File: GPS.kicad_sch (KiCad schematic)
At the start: 14 parts, among them Q5 Q_NMOS_DGS, Q6 Q_PMOS_DGS, U10 L96-M33

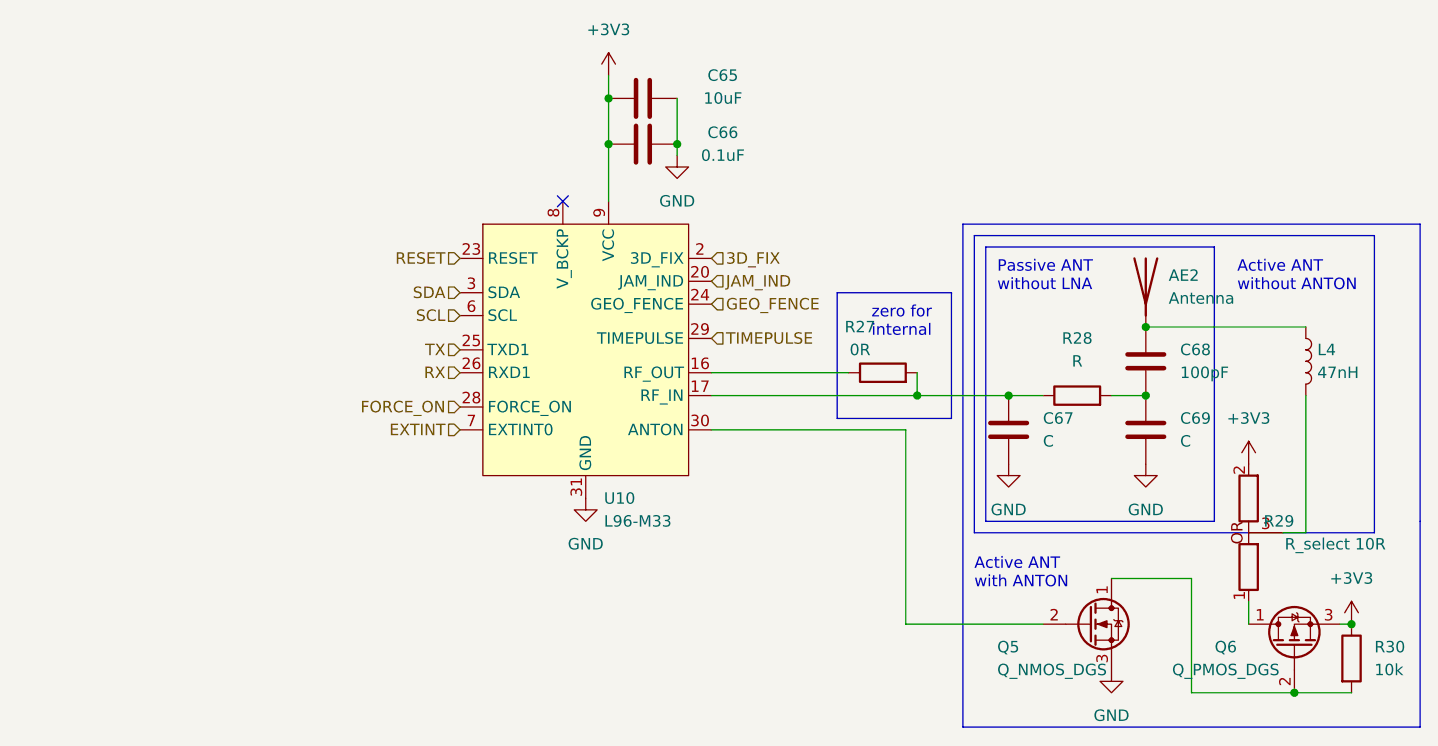
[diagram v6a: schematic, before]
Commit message: added nfc antenna components, added most of footprints
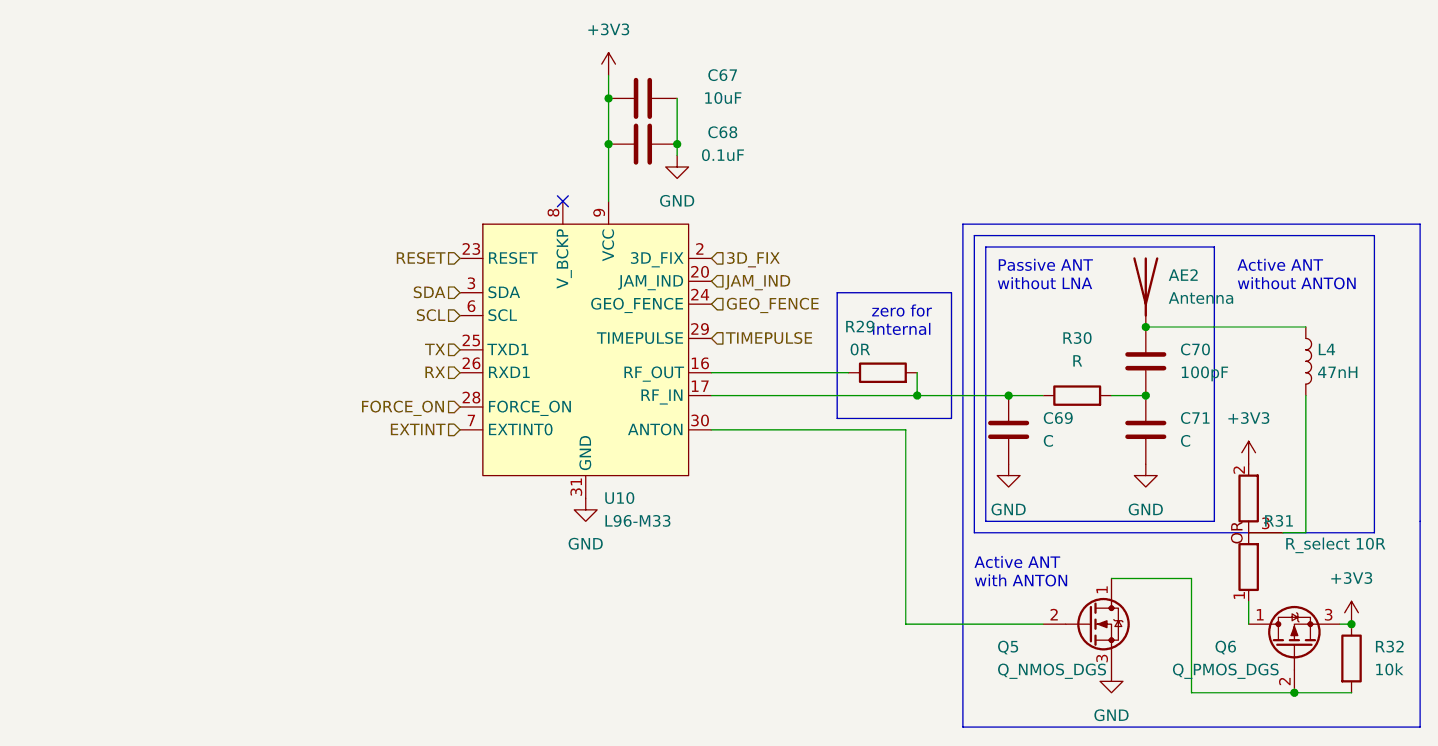
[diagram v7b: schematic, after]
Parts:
- AE2: footprint (none) -> Connector_Coaxial:U.FL_Molex_MCRF_73412-0110_Vertical
- C68: renamed from C66; footprint (none) -> Capacitor_SMD:C_0603_1608Metric_Pad1.08x0.95mm_HandSolder
- C69: renamed from C67; footprint (none) -> Capacitor_SMD:C_0603_1608Metric_Pad1.08x0.95mm_HandSolder
- C70: renamed from C68; footprint (none) -> Capacitor_SMD:C_0603_1608Metric_Pad1.08x0.95mm_HandSolder
- C71: renamed from C69; footprint (none) -> Capacitor_SMD:C_0603_1608Metric_Pad1.08x0.95mm_HandSolder
- R30: renamed from R28; footprint (none) -> Resistor_SMD:R_0603_1608Metric
- R31: renamed from R29; footprint (none) -> airsoft_controller:0603-R-select
- R32: renamed from R30; footprint (none) -> Resistor_SMD:R_0603_1608Metric
- U10: footprint airsoft_controller:L29 -> airsoft_controller:L96
- renumbered C65 to C67, R27 to R29
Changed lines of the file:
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@@
   (symbol (lib_id "Device:R") (at 172.72 90.17 90) (unit 1)
     (in_bom yes) (on_board yes)
-    (property "Reference" "R27" (id 0) (at 170.18 85.09 90))
+    (property "Reference" "R29" (id 0) (at 170.18 85.09 90))
     (property "Value" "0R" (id 1) (at 170.18 87.63 90))
     (property "Footprint" "" (id 2) (at 172.72 91.948 90)
@@
   (symbol (lib_id "Device:C") (at 201.93 88.9 180) (unit 1)
     (in_bom yes) (on_board yes)
-    (property "Reference" "C68" (id 0) (at 205.74 87.6299 0)
+    (property "Reference" "C70" (id 0) (at 205.74 87.6299 0)
       (effects (font (size 1.27 1.27)) (justify right))
     )
@@
       (effects (font (size 1.27 1.27)) (justify right))
     )
-    (property "Footprint" "" (id 2) (at 200.9648 85.09 0)
+    (property "Footprint" "Capacitor_SMD:C_0603_1608Metric_Pad1.08x0.95mm_HandSolder" (id 2) (at 200.9648 85.09 0)
       (effects (font (size 1.27 1.27)) hide)
     )
@@
   (symbol (lib_id "Device:C") (at 146.05 64.77 270) (mirror x) (unit 1)
     (in_bom yes) (on_board yes)
-    (property "Reference" "C66" (id 0) (at 154.94 63.5 90))
+    (property "Reference" "C68" (id 0) (at 154.94 63.5 90))
     (property "Value" "0.1uF" (id 1) (at 154.94 66.04 90))
-    (property "Footprint" "" (id 2) (at 142.24 63.8048 0)
+    (property "Footprint" "Capacitor_SMD:C_0603_1608Metric_Pad1.08x0.95mm_HandSolder" (id 2) (at 142.24 63.8048 0)
       (effects (font (size 1.27 1.27)) hide)
     )
@@
       (effects (font (size 1.27 1.27)) (justify left))
     )
-    (property "Footprint" "" (id 2) (at 201.93 80.01 0)
+    (property "Footprint" "Connector_Coaxial:U.FL_Molex_MCRF_73412-0110_Vertical" (id 2) (at 201.93 80.01 0)
       (effects (font (size 1.27 1.27)) hide)
     )
@@
   (symbol (lib_id "Device:C") (at 201.93 96.52 0) (unit 1)
     (in_bom yes) (on_board yes) (fields_autoplaced)
-    (property "Reference" "C69" (id 0) (at 205.74 95.2499 0)
+    (property "Reference" "C71" (id 0) (at 205.74 95.2499 0)
       (effects (font (size 1.27 1.27)) (justify left))
     )
@@
       (effects (font (size 1.27 1.27)) (justify left))
     )
-    (property "Footprint" "" (id 2) (at 202.8952 100.33 0)
+    (property "Footprint" "Capacitor_SMD:C_0603_1608Metric_Pad1.08x0.95mm_HandSolder" (id 2) (at 202.8952 100.33 0)
       (effects (font (size 1.27 1.27)) hide)
     )
@@
       (effects (font (size 1.27 1.27)) (justify left))
     )
-    (property "Footprint" "airsoft_controller:L29" (id 2) (at 140.97 106.68 0)
+    (property "Footprint" "airsoft_controller:L96" (id 2) (at 140.97 106.68 0)
       (effects (font (size 1.27 1.27)) hide)
     )
@@
   (symbol (lib_id "airsoft_controller:R_select") (at 213.36 107.95 180) (unit 1)
     (in_bom yes) (on_board yes)
-    (property "Reference" "R29" (id 0) (at 218.44 106.68 0)
+    (property "Reference" "R31" (id 0) (at 218.44 106.68 0)
       (effects (font (size 1.27 1.27)) (justify left))
     )
@@
       (effects (font (size 1.27 1.27)) (justify left))
     )
-    (property "Footprint" "" (id 2) (at 213.36 107.95 0)
+    (property "Footprint" "airsoft_controller:0603-R-select" (id 2) (at 213.36 107.95 0)
       (effects (font (size 1.27 1.27)) hide)
     )
@@
   (symbol (lib_id "Device:C") (at 186.69 96.52 0) (unit 1)
     (in_bom yes) (on_board yes) (fields_autoplaced)
-    (property "Reference" "C67" (id 0) (at 190.5 95.2499 0)
+    (property "Reference" "C69" (id 0) (at 190.5 95.2499 0)
       (effects (font (size 1.27 1.27)) (justify left))
     )
@@
       (effects (font (size 1.27 1.27)) (justify left))
     )
-    (property "Footprint" "" (id 2) (at 187.6552 100.33 0)
+    (property "Footprint" "Capacitor_SMD:C_0603_1608Metric_Pad1.08x0.95mm_HandSolder" (id 2) (at 187.6552 100.33 0)
       (effects (font (size 1.27 1.27)) hide)
     )
@@
   (symbol (lib_id "Device:C") (at 146.05 59.69 270) (mirror x) (unit 1)
     (in_bom yes) (on_board yes)
-    (property "Reference" "C65" (id 0) (at 154.94 57.15 90))
+    (property "Reference" "C67" (id 0) (at 154.94 57.15 90))
     (property "Value" "10uF" (id 1) (at 154.94 59.69 90))
     (property "Footprint" "" (id 2) (at 142.24 58.7248 0)
@@
   (symbol (lib_id "Device:R") (at 224.79 121.92 0) (unit 1)
     (in_bom yes) (on_board yes) (fields_autoplaced)
-    (property "Reference" "R30" (id 0) (at 227.33 120.6499 0)
+    (property "Reference" "R32" (id 0) (at 227.33 120.6499 0)
       (effects (font (size 1.27 1.27)) (justify left))
     )
@@
       (effects (font (size 1.27 1.27)) (justify left))
     )
-    (property "Footprint" "" (id 2) (at 223.012 121.92 90)
+    (property "Footprint" "Resistor_SMD:R_0603_1608Metric" (id 2) (at 223.012 121.92 90)
       (effects (font (size 1.27 1.27)) hide)
     )
@@
   (symbol (lib_id "Device:R") (at 194.31 92.71 90) (unit 1)
     (in_bom yes) (on_board yes) (fields_autoplaced)
-    (property "Reference" "R28" (id 0) (at 194.31 86.36 90))
+    (property "Reference" "R30" (id 0) (at 194.31 86.36 90))
     (property "Value" "R" (id 1) (at 194.31 88.9 90))
-    (property "Footprint" "" (id 2) (at 194.31 94.488 90)
-      (effects (font (size 1.27 1.27)) hide)
-    )
+    (property "Footprint" "Resistor_SMD:R_0603_1608Metric" (id 2) (at 194.31 94.488 90)
+      (effects (font (size 1.27 1.27)) hide)
+    )

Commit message: schematic creation
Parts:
- removed AE2: Antenna, Connector_Coaxial:U.FL_Molex_MCRF_73412-0110_Vertical, symbol Device:Antenna
- added AE2: Antenna_Shield, Connector_Coaxial:U.FL_Molex_MCRF_73412-0110_Vertical, symbol Device:Antenna_Shield
- C69: renamed from C67; footprint (none) -> Capacitor_SMD:C_1206_3216Metric_Pad1.33x1.80mm_HandSolder
- L4: footprint (none) -> Inductor_SMD:L_0603_1608Metric_Pad1.05x0.95mm_HandSolder
- Q3: renamed from Q5; footprint (none) -> Package_TO_SOT_SMD:SOT-23; symbol Device:Q_NMOS_DGS -> Device:Q_NMOS_GSD
- Q4: renamed from Q6; footprint (none) -> Package_TO_SOT_SMD:SOT-23; symbol Device:Q_PMOS_DGS -> Device:Q_PMOS_GSD
- R27: renamed from R29; footprint (none) -> Resistor_SMD:R_0603_1608Metric_Pad0.98x0.95mm_HandSolder
- R28: renamed from R30; footprint Resistor_SMD:R_0603_1608Metric -> Resistor_SMD:R_0603_1608Metric_Pad0.98x0.95mm_HandSolder
- R30: renamed from R32; footprint Resistor_SMD:R_0603_1608Metric -> Resistor_SMD:R_0603_1608Metric_Pad0.98x0.95mm_HandSolder
- renumbered C68 to C70, C69 to C71, C70 to C72, C71 to C73, R31 to R29
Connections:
- net +3V3: now also Q4.2 (S); no longer Q4.3 (S)
- net GND: now also Q3.2 (S), AE2.2 (Shield); no longer Q3.3 (S)
- net at C72.2, L4.1: now also AE2.1 (A)
- net at U10.30 (ANTON): now also Q3.1 (G); no longer Q3.2 (G)
- net at Q4.1 (G): now also Q3.3 (D), R30.2; no longer R29.1
- new net: Q4.3 (D), R29.1
